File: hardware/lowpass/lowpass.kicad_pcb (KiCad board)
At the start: 2 copper layers, 50 x 50 mm, 6 parts, among them M1 MountingHole_3.2mm_M3_Pad, M2 MountingHole_3.2mm_M3_Pad, M3 MountingHole_3.2mm_M3_Pad, M4 MountingHole_3.2mm_M3_Pad, P2 OUT, X1 IN

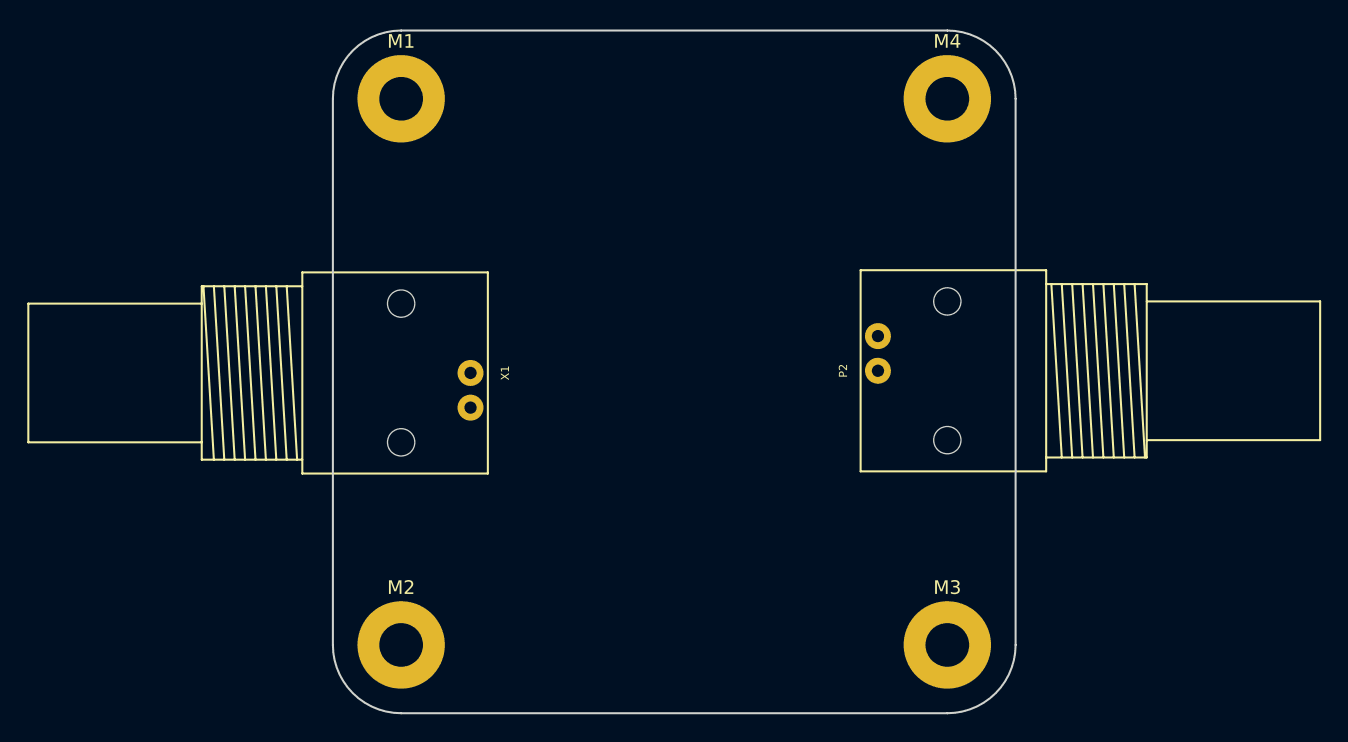
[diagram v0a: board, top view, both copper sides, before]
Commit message: first version of filter layout
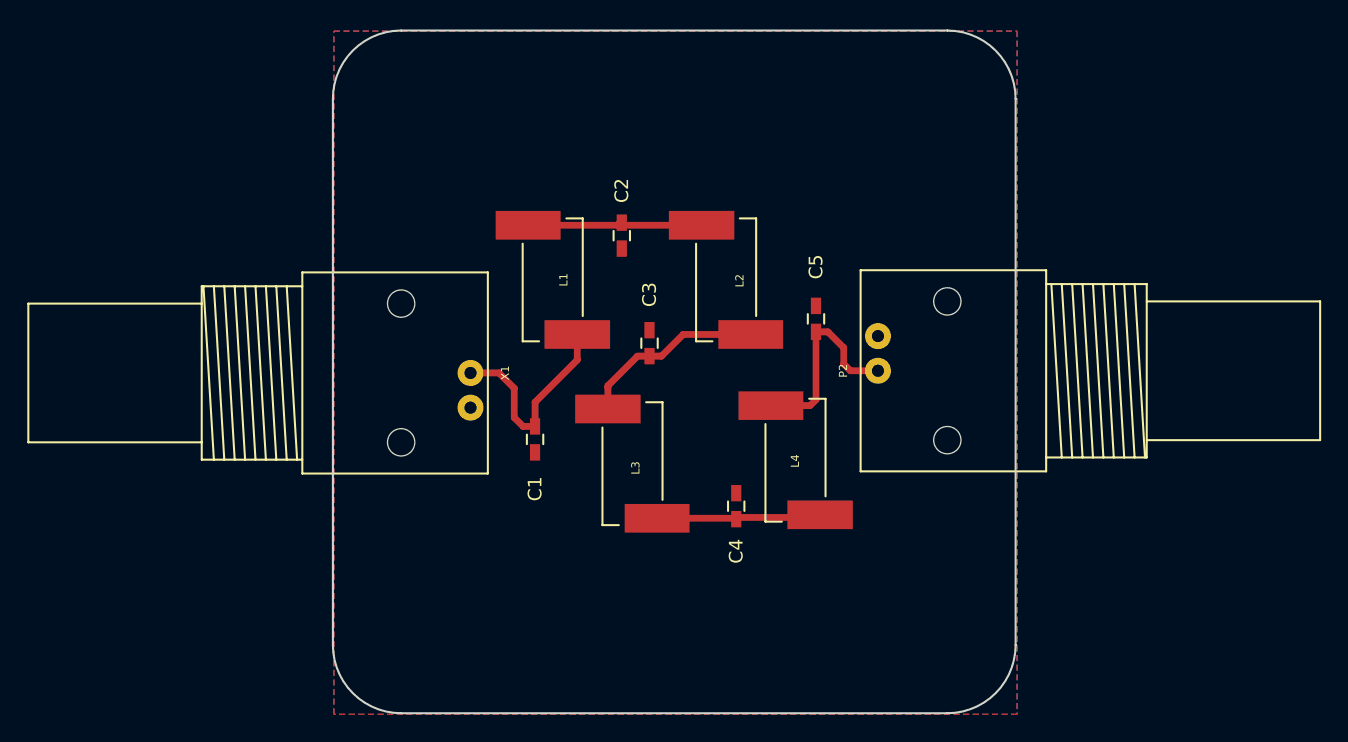
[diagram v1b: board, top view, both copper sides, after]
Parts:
- removed M1, M2, M3, M4: MountingHole_3.2mm_M3_Pad, Mounting_Holes:MountingHole_3.2mm_M3_Pad
- added C1: 82p, Capacitors_SMD:C_0603_HandSoldering, F.Cu at (114.8, 79.9)
- added C2: 180p, Capacitors_SMD:C_0603_HandSoldering, F.Cu at (121.2, 65.0)
- added C3: 180p, Capacitors_SMD:C_0603_HandSoldering, F.Cu at (123.2, 72.9)
- added C4: 180p, Capacitors_SMD:C_0603_HandSoldering, F.Cu at (129.5, 84.8)
- added C5: 82p, Capacitors_SMD:C_0603_HandSoldering, F.Cu at (135.4, 71.1)
- added L1: 307n, projekt5:Coil_132-XXSM_L_, F.Cu at (117.9, 72.3)
- added L2: 380n, projekt5:Coil_132-XXSM_L_, F.Cu at (127.0, 64.3)
- added L3: 380n, projekt5:Coil_132-XXSM_L_, F.Cu at (120.1, 77.7)
- added L4: 307n, projekt5:Coil_132-XXSM_L_, F.Cu at (135.7, 85.5)
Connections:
- P2 pad 2: Net-(P2-Pad2) -> GND
- X1 pad 2: Net-(X1-Pad2) -> GND
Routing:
- net Net-(C1-Pad1): track 0.00 -> 15.6 mm
- net Net-(C5-Pad1): track 0.00 -> 14.9 mm
- net Net-(C3-Pad1): track 0.00 -> 13.7 mm
- net Net-(C2-Pad1): track 0.00 -> 12.8 mm
- net Net-(C4-Pad1): track 0.00 -> 12.0 mm
- added copper zone on B.Cu, net GND
- added copper zone on F.Cu, net GND
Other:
- net class Default: clearance 0.2 -> 0.3; trace_width 0.25 -> 0.5
- rule trace_clearance: 0.2 -> 0.3

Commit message: Fixed long traces in lowpass
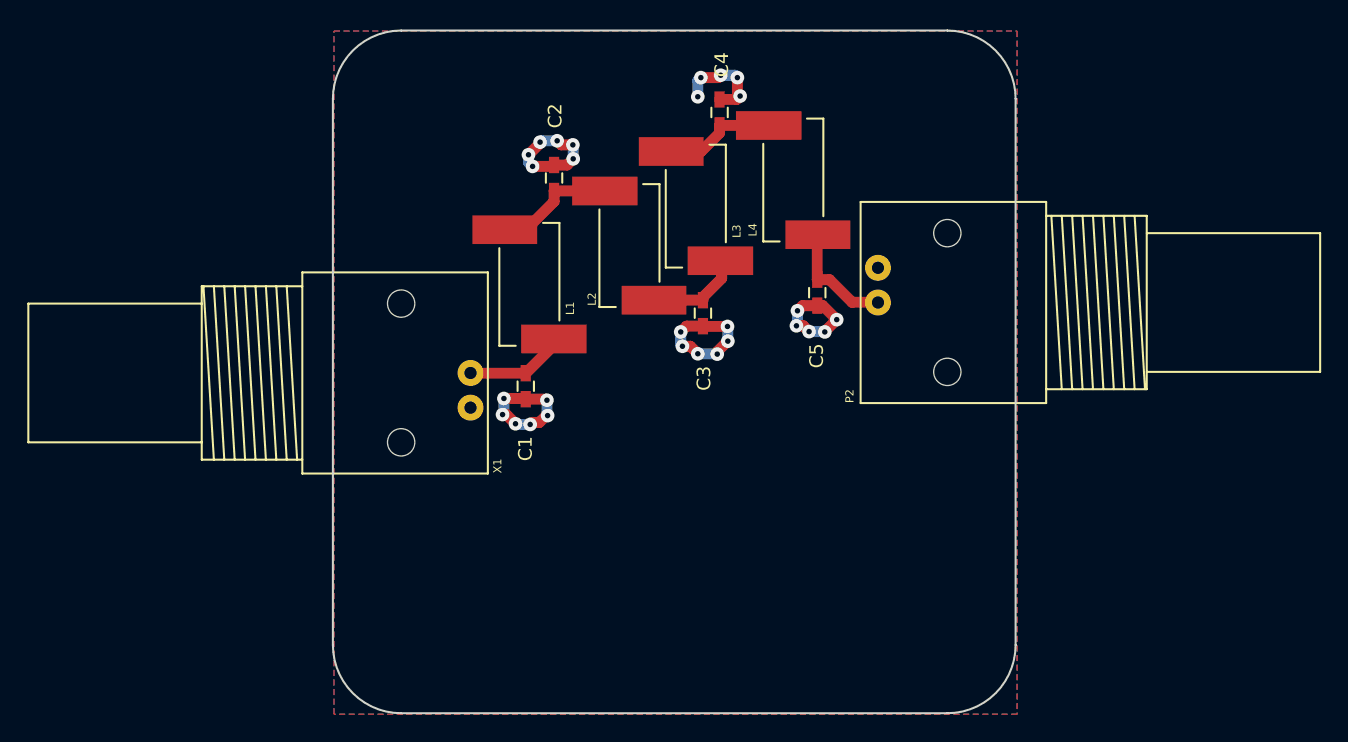
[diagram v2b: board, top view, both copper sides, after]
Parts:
- moved C4 28.9 mm to (128.3, 56.0)
- moved L4 28.8 mm to (131.9, 57.0), turned to 270 degrees
- moved L3 13.6 mm to (128.4, 66.9), turned to 90 degrees
- moved L2 7.51 mm to (119.9, 61.8)
- moved C2 6.51 mm to (116.2, 60.8), turned to 90 degrees
- moved P2 5.00 mm to (139.9, 67.4)
- moved C3 4.49 mm to (127.1, 70.7), turned to 270 degrees
- moved C1 3.95 mm to (114.1, 76.0)
- moved C5 1.92 mm to (135.5, 69.2), turned to 270 degrees
- moved L1 1.74 mm to (116.2, 72.6)
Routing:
- net GND: track 0.00 -> 43.8 mm, vias 0 -> 28
- net Net-(C1-Pad1): track 15.6 -> 7.42 mm
- net Net-(C3-Pad1): track 13.7 -> 7.08 mm
- net Net-(C5-Pad1): track 14.9 -> 8.46 mm
- net Net-(C2-Pad1): track 12.8 -> 8.96 mm
- net Net-(C4-Pad1): track 12.0 -> 8.26 mm
